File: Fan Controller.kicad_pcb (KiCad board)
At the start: 2 copper layers, 33 x 96 mm, 37 parts, among them J1 Power Input, J2 4-Pin Fan Header, J3 4-Pin Fan Header, J4 I2C, J5 Conn_01x04, J6 Conn_01x06, J7 Conn_01x05, Q1 SQD19P06-60L_GE3, U1 ESP32-C3-SuperMini, U2 AP63205QWU-7, U3 SN74LVC2G06DBVR

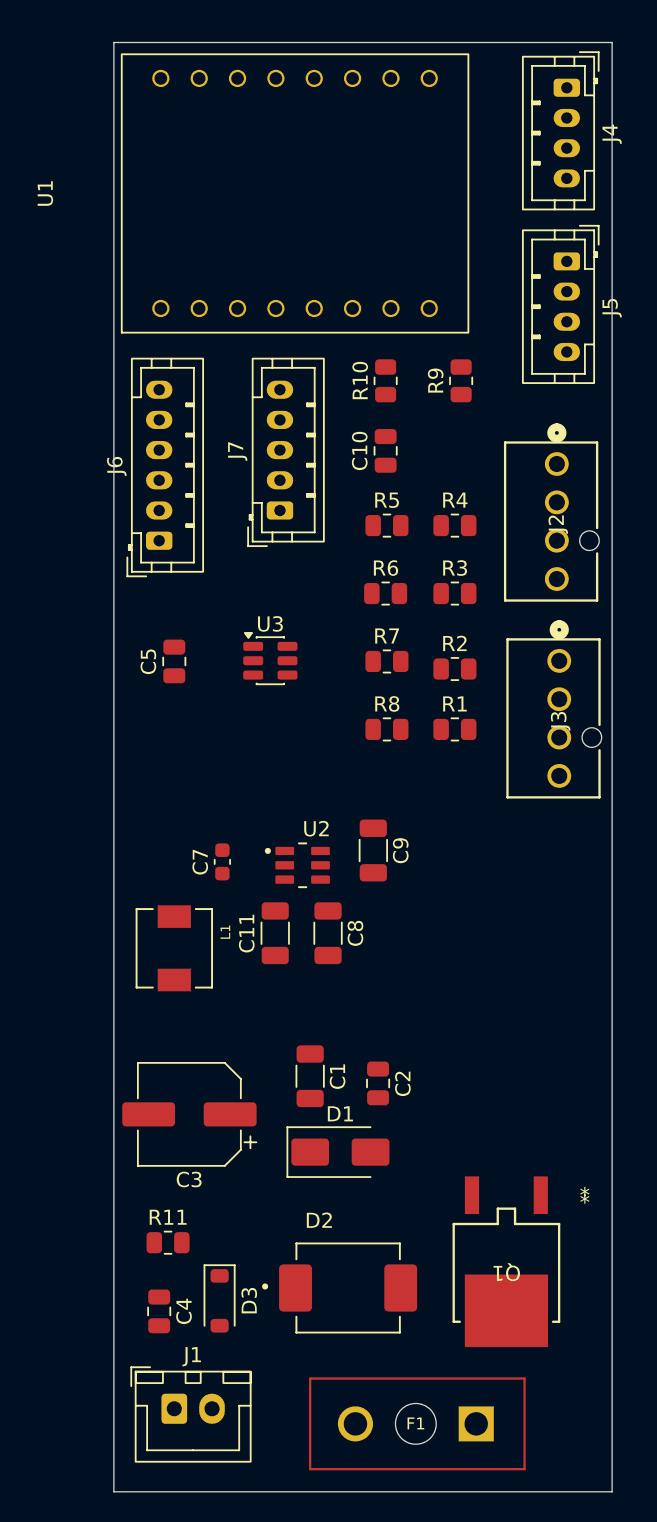
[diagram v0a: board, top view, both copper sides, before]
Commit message: PCB: fix L1 land pattern, move F1 outline off copper, re-place all sections
Co-authored-by: radovanobal <60649057+radovanobal@users.noreply.github.com>
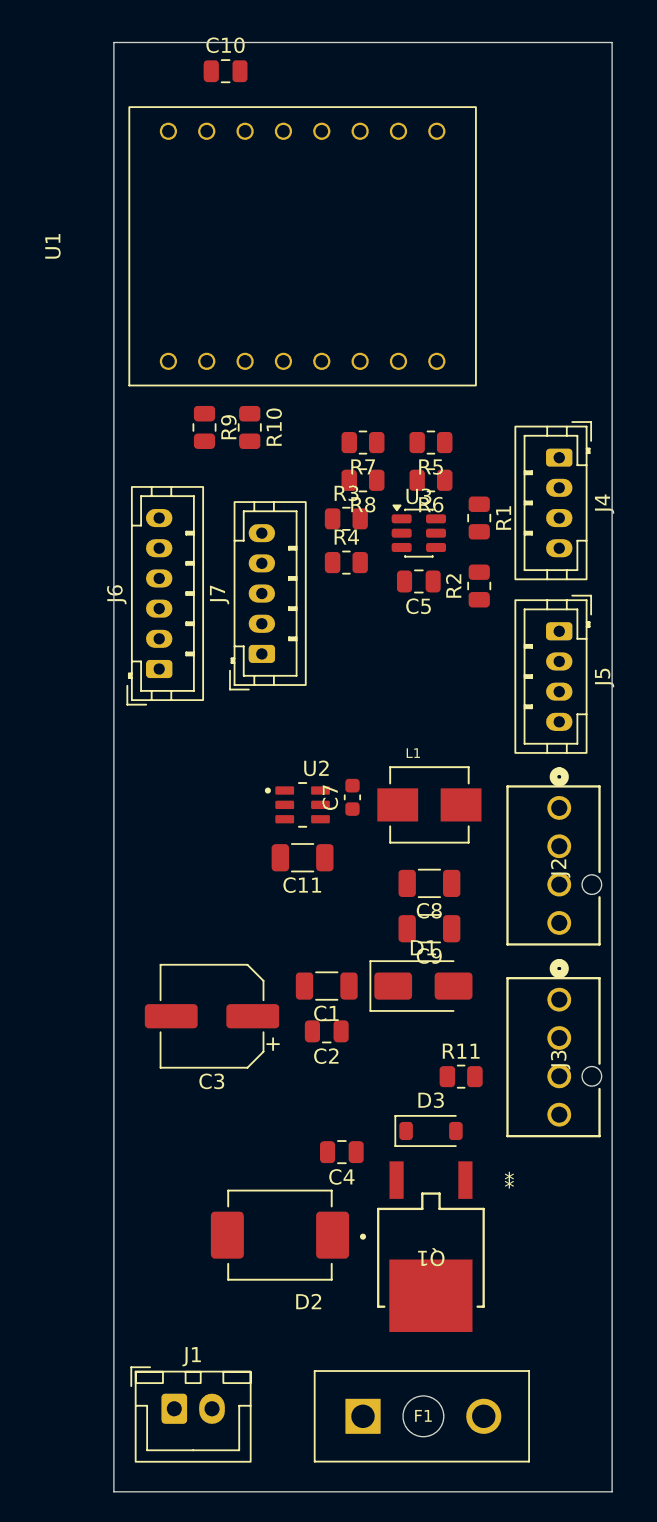
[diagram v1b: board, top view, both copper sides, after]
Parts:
- moved C10 27.3 mm to (158.9, 39.4), turned to 0 degrees
- moved J4 24.5 mm to (181.0, 65.0)
- moved J5 24.5 mm to (181.0, 76.5)
- moved J2 22.8 mm to (181.0, 88.2)
- moved J3 22.4 mm to (181.0, 100.9)
- moved R11 22.3 mm to (174.5, 106.0)
- moved L1 19.4 mm to (172.4, 88.0), turned to 0 degrees
- moved D3 18.0 mm to (172.5, 109.6), turned to 0 degrees
- moved R9 17.3 mm to (157.5, 63.0), turned to 270 degrees
- moved C5 17.0 mm to (171.7, 73.2), turned to 180 degrees
- moved R8 16.6 mm to (168.0, 66.5), turned to 180 degrees
- moved C4 16.1 mm to (166.6, 111.0), turned to 180 degrees
- moved R7 14.6 mm to (168.0, 64.0), turned to 180 degrees
- moved R1 14.1 mm to (175.7, 69.0), turned to 270 degrees
- moved U3 13.0 mm to (171.7, 70.0)
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
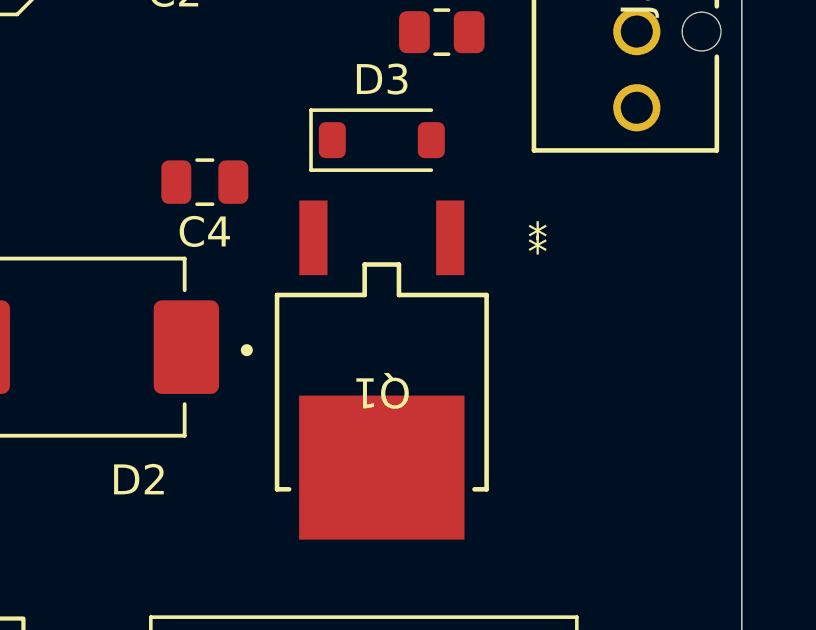
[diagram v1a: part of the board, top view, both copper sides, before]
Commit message: PCB: normalize silk text angles, add antenna keepout annotation
Co-authored-by: radovanobal <60649057+radovanobal@users.noreply.github.com>
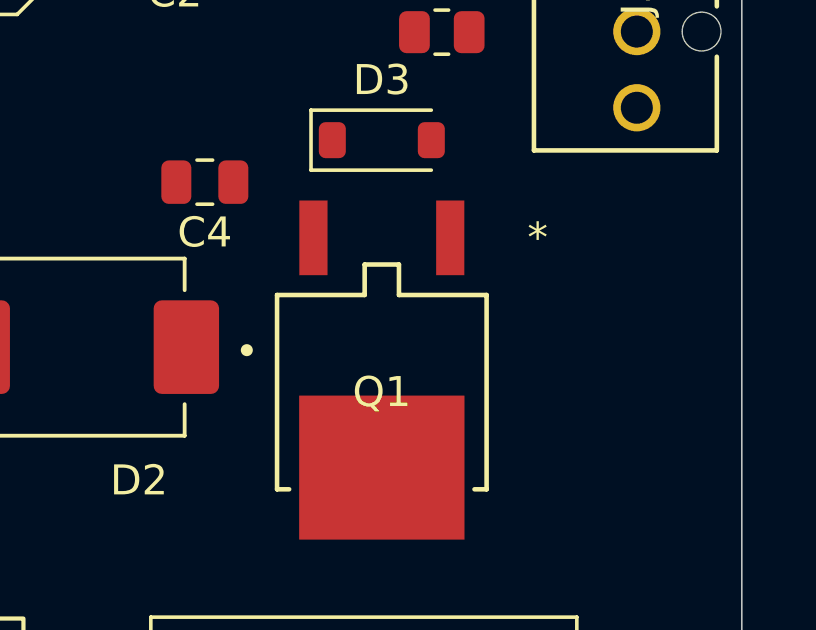
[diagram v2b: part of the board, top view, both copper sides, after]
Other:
- board text added: "ANTENNA KEEPOUT"

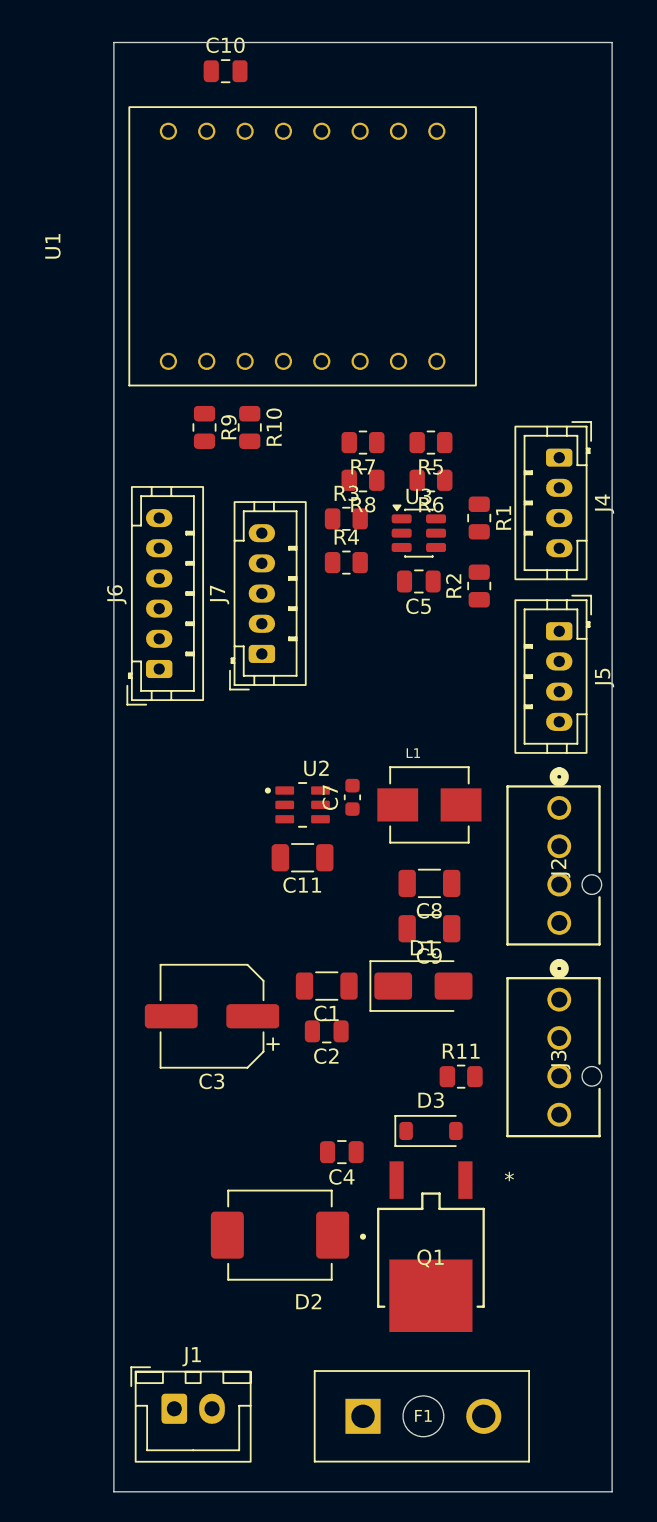
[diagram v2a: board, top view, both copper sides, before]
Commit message: PCB: rotate U1 180 deg so antenna faces board edge, clear USB corridor
Co-authored-by: radovanobal <60649057+radovanobal@users.noreply.github.com>
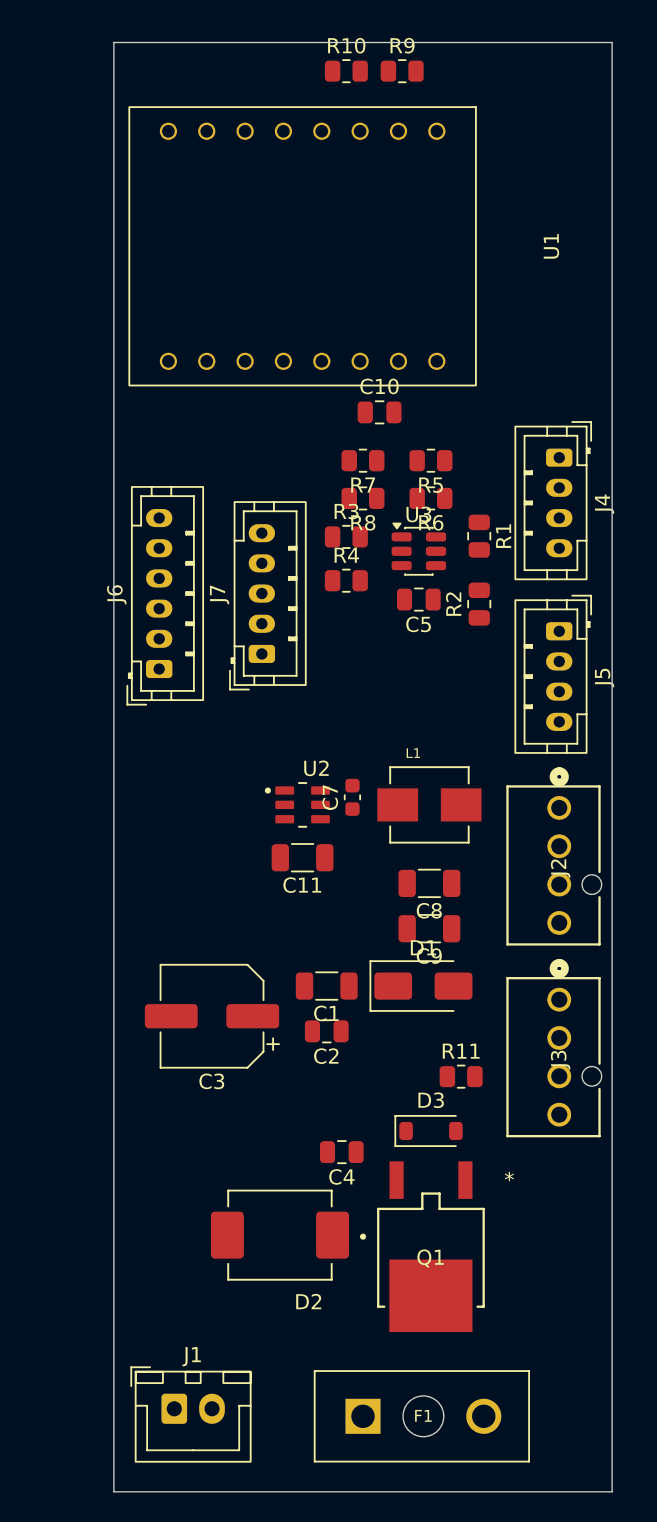
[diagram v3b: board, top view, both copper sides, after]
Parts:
- moved R9 27.0 mm to (170.6, 39.4), turned to 0 degrees
- moved C10 24.8 mm to (169.1, 62.0)
- moved R10 24.5 mm to (166.9, 39.4), turned to 0 degrees
- moved C5 1.20 mm to (171.7, 74.4)
- moved R1 1.20 mm to (175.7, 70.2)
- moved R2 1.20 mm to (175.7, 74.7)
- moved R3 1.20 mm to (166.9, 70.2)
- moved R4 1.20 mm to (166.9, 73.2)
- moved R5 1.20 mm to (172.5, 65.2)
- moved R6 1.20 mm to (172.5, 67.7)
- moved R7 1.20 mm to (168.0, 65.2)
- moved R8 1.20 mm to (168.0, 67.7)
- moved U3 1.20 mm to (171.7, 71.2)
- turned U1 to 270 degrees
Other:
- board text added: "USB ACCESS"

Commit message: PCB: optimization pass - tighten critical loops, align rows, fix silk ref overlaps
Co-authored-by: radovanobal <60649057+radovanobal@users.noreply.github.com>
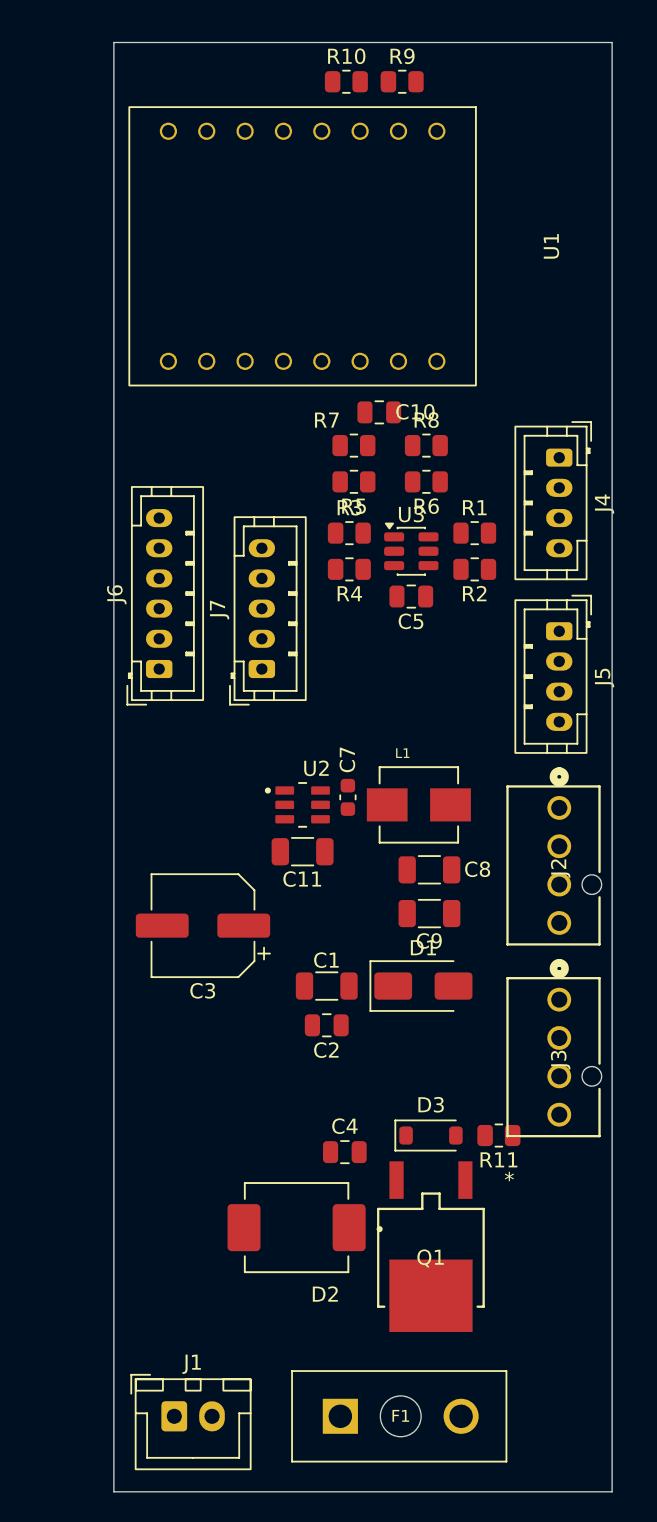
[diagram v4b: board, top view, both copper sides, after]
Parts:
- moved C3 6.03 mm to (157.4, 96.0)
- moved R8 5.47 mm to (172.2, 64.2), turned to 0 degrees
- moved R5 5.29 mm to (167.4, 66.6)
- moved R11 4.63 mm to (177.0, 109.9), turned to 180 degrees
- moved R2 2.32 mm to (175.4, 72.4), turned to 180 degrees
- moved F1 1.50 mm to (170.5, 128.5)
- moved D2 1.21 mm to (163.6, 116.0)
- moved R7 1.17 mm to (167.4, 64.2), turned to 0 degrees
- moved R6 1.14 mm to (172.2, 66.6)
- moved C9 1.00 mm to (172.4, 95.2)
- moved J7 1.00 mm to (161.3, 79.0)
- moved C8 0.90 mm to (172.4, 92.3)
- moved R4 0.78 mm to (167.1, 72.4)
- moved L1 0.70 mm to (171.7, 88.0)
- moved R10 0.70 mm to (166.9, 40.1)
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
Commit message: silk reposition, overlap fix
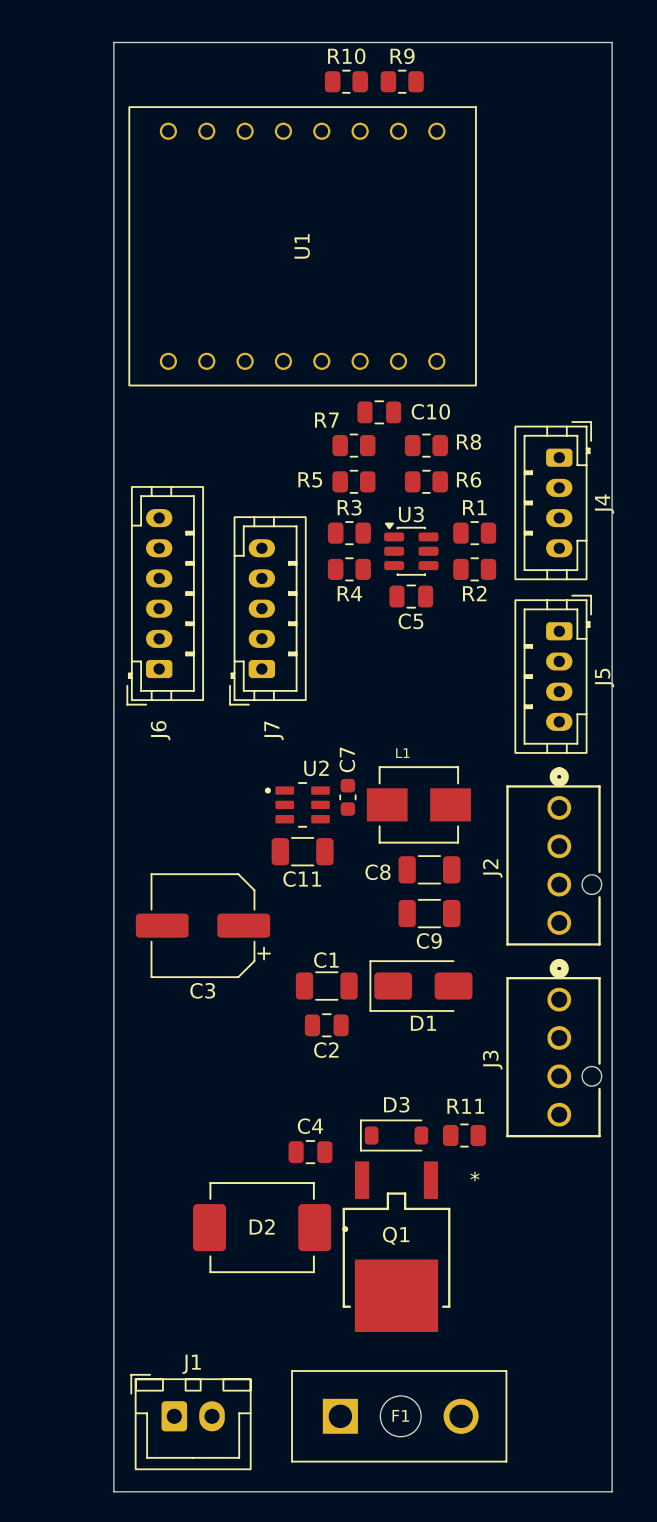
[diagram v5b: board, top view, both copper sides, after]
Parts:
- moved C4 2.28 mm to (164.5, 111.0)
- moved D2 2.28 mm to (161.3, 116.0)
- moved D3 2.28 mm to (170.2, 109.9)
- moved Q1 2.28 mm to (170.2, 118.0)
- moved R11 2.28 mm to (174.7, 109.9)

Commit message: Routed the placements
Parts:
- moved D2 1.55 mm to (159.8, 116.0)
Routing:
- net GND: track 0.00 -> 97.3 mm, vias 0 -> 1
- net /FAN1_PWM_GPIO: track 0.00 -> 59.1 mm, vias 0 -> 1
- net /+5V_SYS: track 0.00 -> 57.2 mm, vias 0 -> 1
- net /GPIO5: track 0.00 -> 53.7 mm
- net /I2C_SCL: track 0.00 -> 50.3 mm
- net /I2C_SDA: track 0.00 -> 47.7 mm
- net /+12V_PROTECTED: track 0.00 -> 46.6 mm, vias 0 -> 4
- net Net-(J3-Pin_3): track 0.00 -> 44.5 mm, vias 0 -> 1
- net /FAN2_PWM_GPIO: track 0.00 -> 44.1 mm, vias 0 -> 1
- net /+3V3: track 0.00 -> 39.2 mm, vias 0 -> 1
- net Net-(J2-Pin_3): track 0.00 -> 38.9 mm, vias 0 -> 1
- net /FAN2_PWM: track 0.00 -> 38.1 mm, vias 0 -> 1
- net /GPIO10: track 0.00 -> 32.6 mm
- net /GPIO8: track 0.00 -> 32.1 mm
- net /12V_RAW_FUSED: track 0.00 -> 29.6 mm, vias 0 -> 3
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- added copper zone on In2.Cu, net /+12V_PROTECTED
- added copper zone on In2.Cu, net /+3V3
- added copper zone on In1.Cu, net GND
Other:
- copper layers 2 -> 4
